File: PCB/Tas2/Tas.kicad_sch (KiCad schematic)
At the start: 25 parts, among them J1 Shelly 1, J2 Conn_01x07, J3 USB-C, Q1 PMF170XP,115, Q2 2N7002BKS, U2 LMR16006YDDCR, U3 CH340X

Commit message: Starting new Tas2
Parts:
- removed Q2: 2N7002BKS, RevK:SOT-363_SC-70-6, symbol Transistor_FET:FDG1024NZ
- removed R8: 4k7, RevK:R_0603, symbol Device:R
- removed R9: 10k, RevK:R_0603, symbol Device:R
- removed U3: CH340X, RevK:CH340X, symbol RevK:CH340X
- added C1: 100nF, RevK:C_0603, symbol Device:C
- added Q2: PMF250XNEX, RevK:SOT-323_SC-70, symbol RevK:NX7002AK
- added R3, R4: 27R, RevK:R_0603, symbol Device:R
- added U1: FT231XQ, RevK:QFN-20-1EP_4x4mm_P0.5mm_EP2.5x2.5mm, symbol RevK:FT231XQ
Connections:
- net D+: now also R4.2, U1.8 (USBDP); no longer J3.A6 (D+), J3.B6 (D+)
- net D-: now also R3.2, U1.9 (USBDM); no longer J3.A7 (D-), J3.B7 (D-)
- net GND: now also C1.2, Q2.2 (S), U1.13 (GND), U1.2 (~{RI}), U1.21 (GND), U1.3 (GND), U1.4 (~{DSR}), U1.5 (~{DCD}), U1.6 (~{CTS})
- net GPIO0: now also U1.18 (~{DTR})
- net RST: now also Q1.1 (G), Q2.1 (G), U1.19 (~{RTS})
- net RXD: now also U1.17 (TXD); no longer D3.1 (K)
- net TXD: now also U1.1 (RXD)
- net VBUS: now also U1.12 (VCC)
- net at J1.3 (Pin_3), J2.3 (Pin_3), Q1.3 (D): now also Q2.3 (D)
- new net: J3.A6 (D+), J3.B6 (D+), R4.1
- new net: J3.A7 (D-), J3.B7 (D-), R3.1
- new net: C1.1, U1.10 (3V3OUT), U1.11 (~{RESET}), U1.20 (VCCIO)
- new net: D3.1 (K), U1.15 (CBUS0)
- no-connect marks 1 -> 4
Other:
- note added: "Configure FTDI - Inverted RTS - CBUS0 mode 9"
- note added: "Note, a better regulator for this may be the TLV62569 as it is suitable up to 5.5V input and small footprint."
- moved on the sheet: C5, D3, J1, J2, Q1, R5

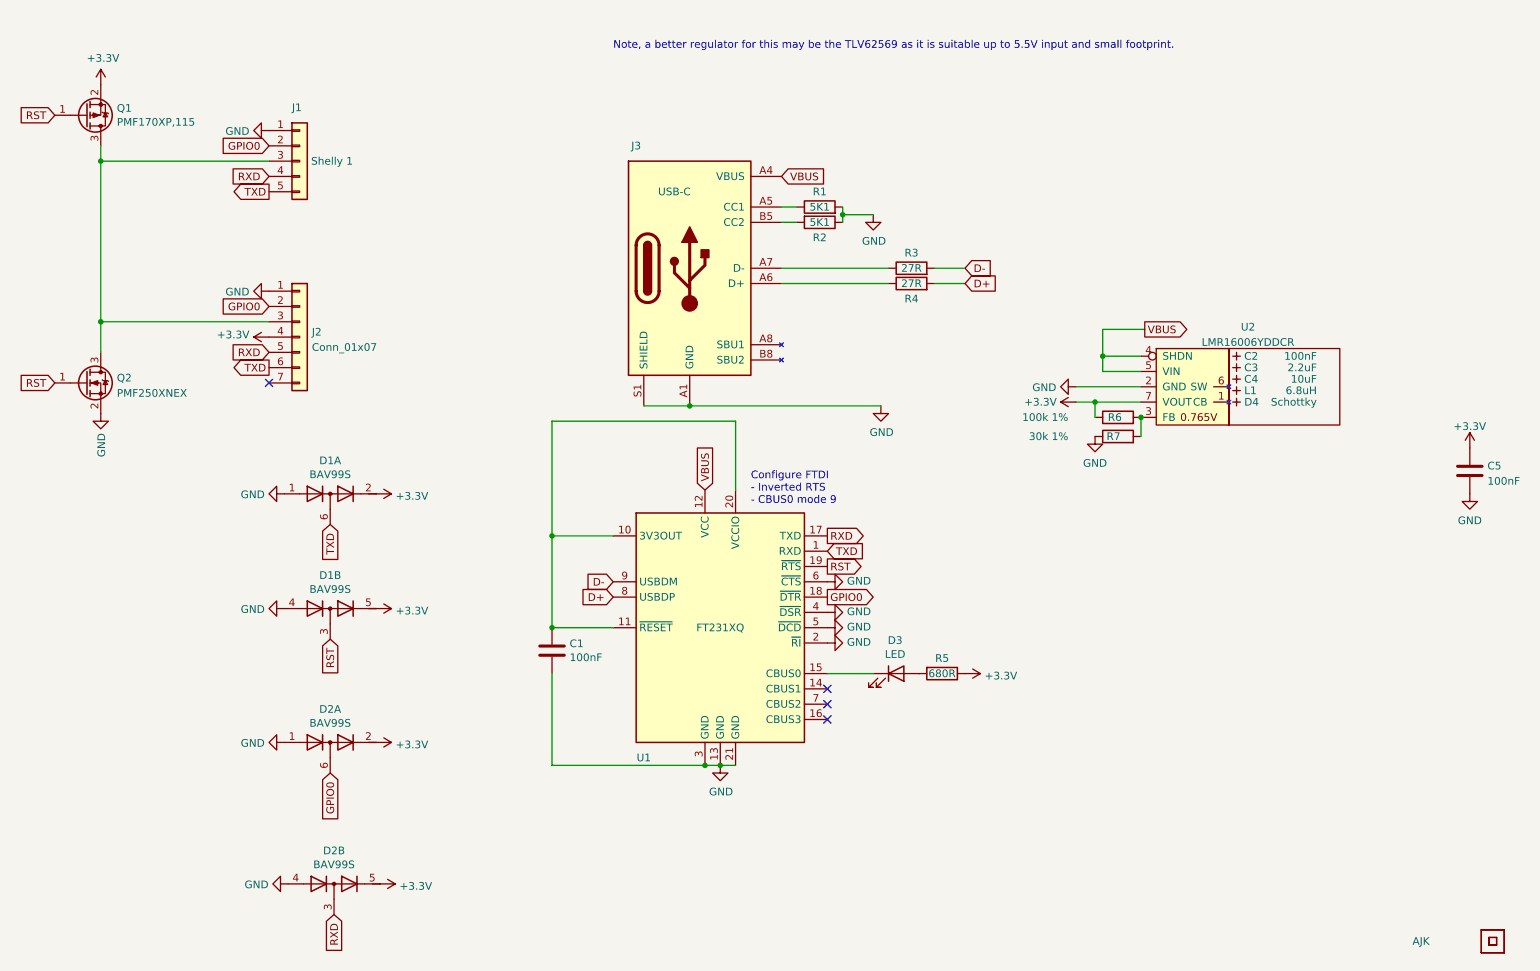
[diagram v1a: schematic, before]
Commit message: Started on new board using FTDI chip
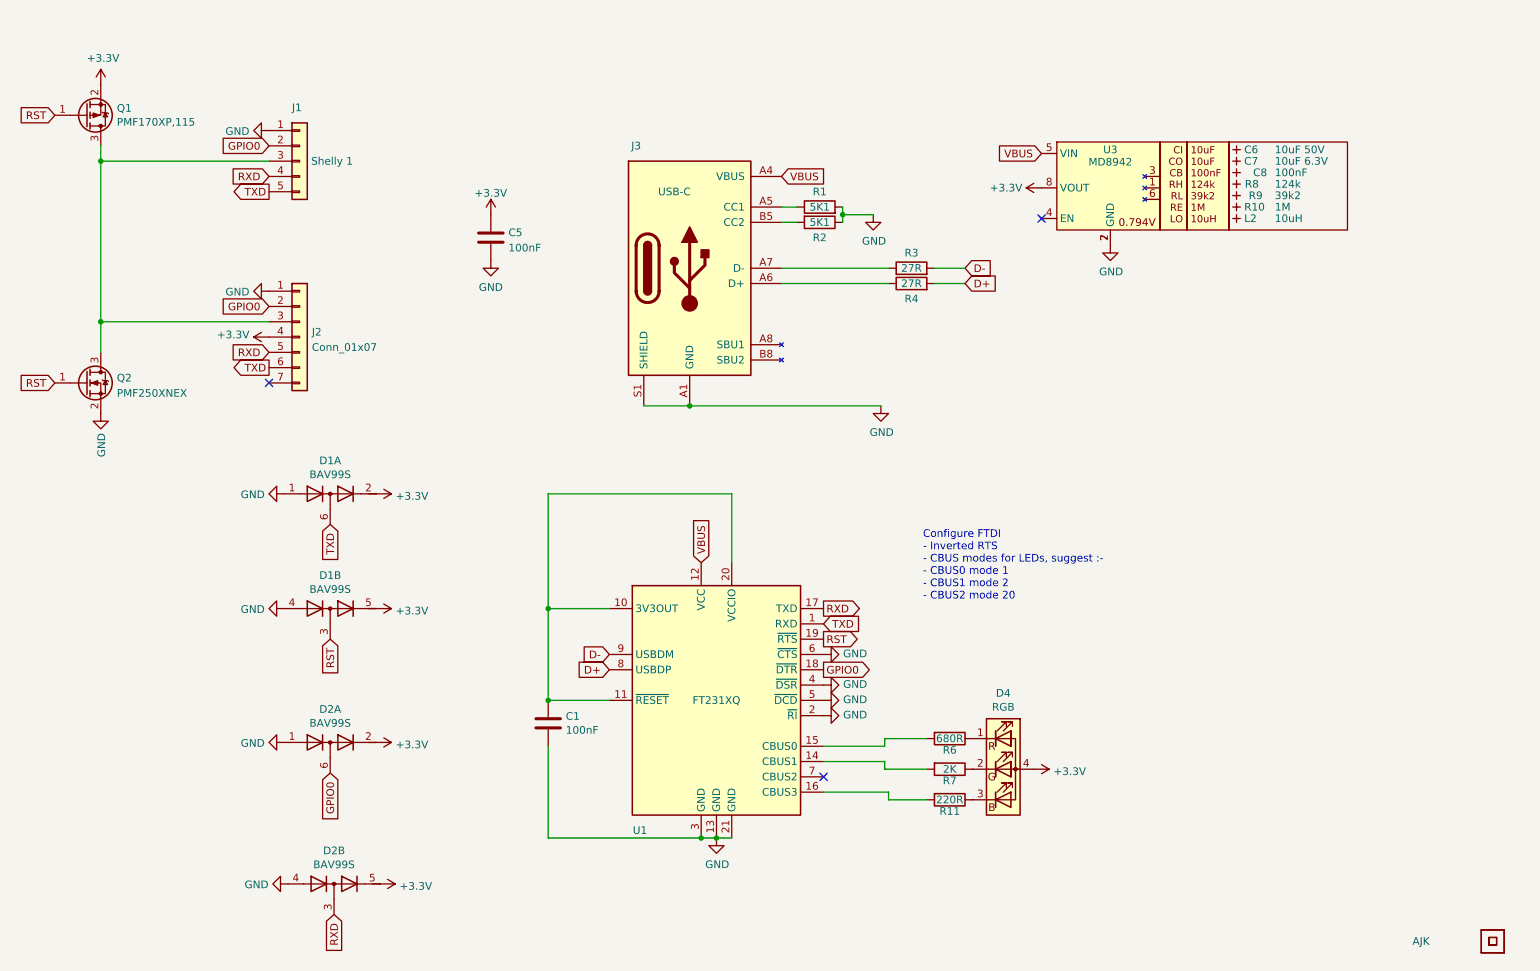
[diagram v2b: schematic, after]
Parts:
- removed C2: 100nF, RevK:C_0603_, symbol RevK:Hidden
- removed C3: 2.2uF, RevK:C_0805_, symbol RevK:Hidden
- removed C4: 10uF, RevK:C_0805_, symbol RevK:Hidden
- removed D3: LED, LED_SMD:LED_0603_1608Metric_Pad1.05x0.95mm_HandSolder, symbol Device:LED
- removed D4: Schottky, RevK:D_1206_, symbol RevK:Hidden
- removed L1: 6.8uH, RevK:L_4x4_, symbol RevK:Hidden
- removed R5: 680R, RevK:R_0603, symbol Device:R
- removed U2: LMR16006YDDCR, RevK:SOT-23-Thin-6-Reg, symbol RevK:LMR16006XDDCR
- added C6: 10uF 50V, RevK:C_0603_, symbol RevK:Hidden
- added C7: 10uF 6.3V, RevK:C_0603_, symbol RevK:Hidden
- added C8: 100nF, RevK:C_0603_, symbol RevK:Hidden
- added D4: RGB, RevK:LED-RGB-1.6x1.6, symbol Device:LED_RGBA
- added L2: 10uH, RevK:L_4x4_, symbol RevK:Hidden
- added R10: 1M, RevK:R_0402_, symbol RevK:Hidden
- added R11: 220R, RevK:R_0402, symbol Device:R
- added R8: 124k, RevK:R_0402_, symbol RevK:Hidden
- added R9: 39k2, RevK:R_0402_, symbol RevK:Hidden
- added U3: MD8942, RevK:SOT-23-6-MD8942, symbol RevK:MD89420-RegBlock
- C1, C5: footprint RevK:C_0603 -> RevK:C_0402
- R1, R2, R3, R4: footprint RevK:R_0603 -> RevK:R_0402
- R6: value 100k 1% -> 680R; footprint RevK:R_0603 -> RevK:R_0402; LCSC Part # C14675 -> (none)
- R7: value 30k 1% -> 2K; footprint RevK:R_0603 -> RevK:R_0402; LCSC Part # C100001 -> (none)
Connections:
- net +3V3: now also D4.4 (A), U3.8 (VOUT); no longer R6.1
- net GND: now also U3.2 (GND), U3.7 (GND); no longer R7.1
- net VBUS: now also U3.5 (VIN)
- net at U1.14 (CBUS1): now also R7.2
- net at U1.15 (CBUS0): now also R6.2
- net at U1.16 (CBUS3): now also R11.2
- new net: D4.1 (RK), R6.1
- new net: D4.2 (GK), R7.1
- new net: D4.3 (BK), R11.1
- no-connect marks 4 -> 3
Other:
- note added: "Configure FTDI - Inverted RTS - CBUS modes for LEDs, suggest :- - CBUS0 mode 1 - CBUS1 mode 2 - CBUS2 mode 20"
- note removed: "Configure FTDI - Inverted RTS - CBUS0 mode 9"
- note removed: "Note, a better regulator for this may be the TLV62569 as it is suitable up to 5.5V input and small footprint."
- moved on the sheet: C1, C5, U1

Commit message: Tracked
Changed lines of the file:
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@@
   (symbol (lib_id "RevK:Hidden") (at 229.235 48.895 270) (unit 1)
     (in_bom yes) (on_board yes) (dnp no)
-    (property "Reference" "R9" (at 232.41 48.895 90)
+    (property "Reference" "R9" (at 231.775 48.895 90)
       (effects (font (size 1.27 1.27)))
     )
@@
   (symbol (lib_id "RevK:Hidden") (at 229.235 45.085 90) (unit 1)
     (in_bom yes) (on_board yes) (dnp no)
-    (property "Reference" "C8" (at 234.315 45.085 90)
+    (property "Reference" "C8" (at 233.045 45.085 90)
       (effects (font (size 1.27 1.27)) (justify left))
     )

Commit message: Tidy tracks
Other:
- note added: "Configure FTDI - Inverted RTS - CBUS modes for LEDs, suggest :- - CBUS0 mode 1 - CBUS1 mode 2 - CBUS3 mode 20"
- note removed: "Configure FTDI - Inverted RTS - CBUS modes for LEDs, suggest :- - CBUS0 mode 1 - CBUS1 mode 2 - CBUS2 mode 20"
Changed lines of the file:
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@@
     (stroke (width 0) (type default))
   )
-  (text "Configure FTDI\n- Inverted RTS\n- CBUS modes for LEDs, suggest :-\n- CBUS0 mode 1\n- CBUS1 mode 2\n- CBUS2 mode 20"
+  (text "Configure FTDI\n- Inverted RTS\n- CBUS modes for LEDs, suggest :-\n- CBUS0 mode 1\n- CBUS1 mode 2\n- CBUS3 mode 20"
     (at 177.165 116.205 0)
     (effects (font (size 1.27 1.27)) (justify left bottom))

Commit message: FTDI fix
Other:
- note added: "Configure FTDI - Inverted RTS - CBUS modes for LEDs, suggest :- - CBUS0 mode 1 - CBUS1 mode 2 - CBUS3 mode 9"
- note removed: "Configure FTDI - Inverted RTS - CBUS modes for LEDs, suggest :- - CBUS0 mode 1 - CBUS1 mode 2 - CBUS3 mode 20"
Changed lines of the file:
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@@
     (stroke (width 0) (type default))
   )
-  (text "Configure FTDI\n- Inverted RTS\n- CBUS modes for LEDs, suggest :-\n- CBUS0 mode 1\n- CBUS1 mode 2\n- CBUS3 mode 20"
+  (text "Configure FTDI\n- Inverted RTS\n- CBUS modes for LEDs, suggest :-\n- CBUS0 mode 1\n- CBUS1 mode 2\n- CBUS3 mode 9"
     (at 177.165 116.205 0)
     (effects (font (size 1.27 1.27)) (justify left bottom))
